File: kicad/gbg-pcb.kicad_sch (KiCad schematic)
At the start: 70 parts, among them J1 12 2.54mm pitch header pins, J100 0197054001, J101 0197054001, J102 0197054001, J103 0197054001, J104 2159151002, J11 Conn_01x10_Pin, J2 Conn_01x04, J3 joystick, J4 speed knob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

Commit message: reviewed
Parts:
- U3: DigiKey_Part_Number 296-44396-1-ND -> (none)
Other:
- moved on the sheet: 3V1, B1, B2, B3, B4, C1, C2, C4, D1, D13, D2, H1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

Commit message: v2.1
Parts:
- R4: value 590k -> 100k; Manufacturer_Part_Number CRCW0805590KFKEA -> CRCW0805100KFKEA; digikey_part_number 541-590KCCT-ND -> 541-100KCCT-ND
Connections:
- net GND: no longer B1.4, B2.4, B3.4, B4.4
- no-connect marks 16 -> 20

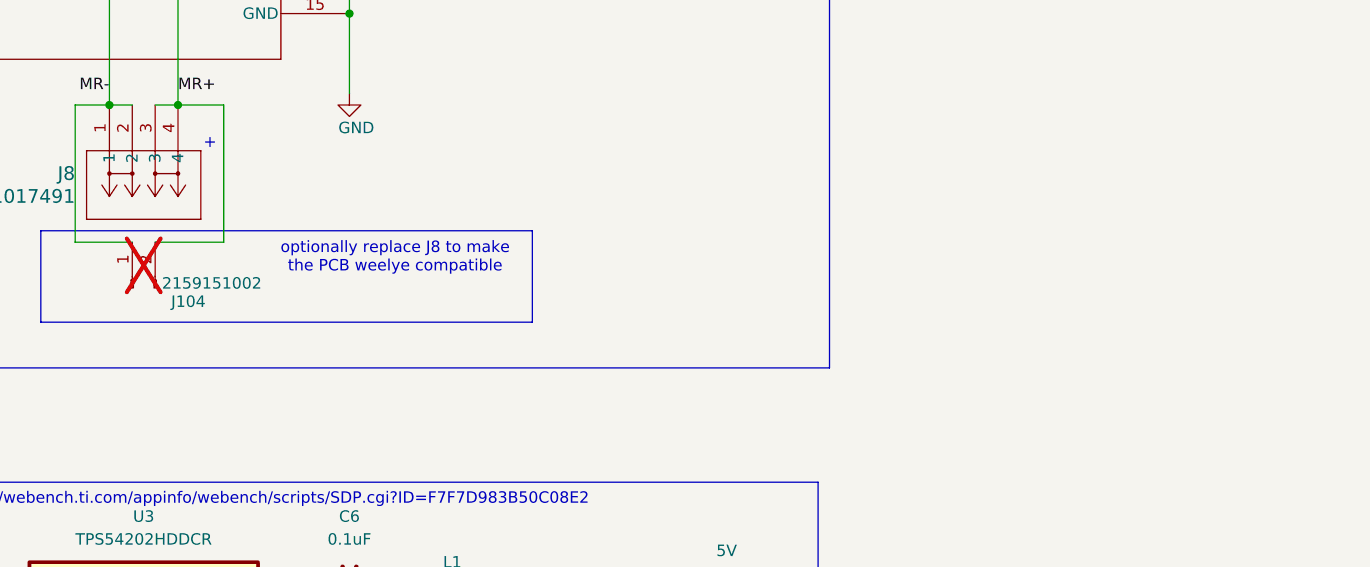
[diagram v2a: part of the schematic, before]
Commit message: add vias
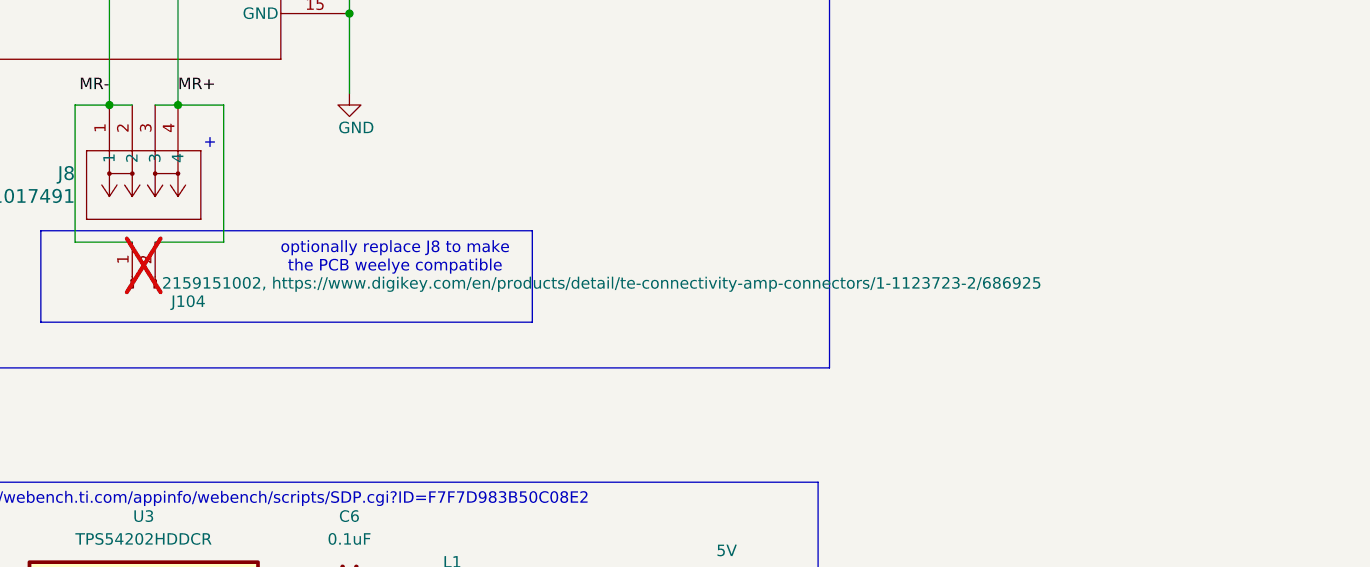
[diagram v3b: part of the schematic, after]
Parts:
- J104: value 2159151002 -> 2159151002, https://www.digikey.com/en/products/detail/te-connectivity-amp-connectors/1-1123723-2/686925
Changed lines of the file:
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@@
 			)
 		)
-		(property "Value" "2159151002"
+		(property "Value" "2159151002, https://www.digikey.com/en/products/detail/te-connectivity-amp-connectors/1-1123723-2/686925"
 			(at 327.152 181.102 90)
 			(show_name no)
@@
 			)
 		)
-		(property "Datasheet" "https://www.digikey.com/en/products/detail/molex/2159151002/16591336"
+		(property "Datasheet" "https://www.digikey.com/en/products/detail/molex/2159151002/16591336, https://www.digikey.com/en/products/detail/te-connectivity-amp-connectors/1-1123723-2/686925"
 			(at 323.85 181.61 0)
 			(hide yes)

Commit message: work on right motor connection
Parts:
- added J105: wellye RX25 style, kicad libraries:TE_1-1123723-2, symbol Connector:Conn_01x02_Pin
- J104: value 2159151002, https://www.digikey.com/en/products/detail/te-connectivity-amp-connectors/1-1123723-2/686925 -> wellye style
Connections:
- net MR+: now also J105.2 (Pin_2)
- net MR-: now also J105.1 (Pin_1)
- net right_1: now also P1.22 (GP17); no longer P1.21 (GP16)
- net right_2: now also P1.21 (GP16); no longer P1.22 (GP17)
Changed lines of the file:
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@@
 	(rectangle
 		(start 313.69 175.26)
-		(end 368.3 185.42)
+		(end 368.3 198.12)
 		(stroke
 			(width 0)
@@
 		)
 	)
-	(text_box "right motor"
-		(exclude_from_sim no)
-		(at 236.22 101.6 0)
-		(size 165.1 88.9)
-		(margins 0.9525 0.9525 0.9525 0.9525)
-		(stroke
-			(width 0)
-			(type solid)
-		)
-		(fill
-			(type none)
-		)
-		(effects
-			(font
-				(size 1.27 1.27)
-			)
-			(justify left top)
-		)
-	)
 	(text_box "qwiic I2C plug"
 		(exclude_from_sim no)
@@
 	)
 	(junction
+		(at 334.01 176.53)
+		(diameter 0)
+		(color 0 0 0 0)
+	)
+	(junction
 		(at 92.71 46.99)
 		(diameter 0)
@@
 	)
 	(junction
+		(at 317.5 176.53)
+		(diameter 0)
+		(color 0 0 0 0)
+	)
+	(junction
 		(at 297.18 50.8)
 		(diameter 0)
@@
 	(wire
 		(pts
+			(xy 317.5 186.69) (xy 317.5 176.53)
+		)
+		(stroke
+			(width 0)
+			(type default)
+		)
+	)
+	(wire
+		(pts
 			(xy 82.55 57.15) (xy 82.55 54.61)
 		)
@@
 	(wire
 		(pts
+			(xy 326.39 186.69) (xy 334.01 186.69)
+		)
+		(stroke
+			(width 0)
+			(type default)
+		)
+	)
+	(wire
+		(pts
 			(xy 102.87 77.47) (xy 102.87 54.61)
 		)
@@
 	(wire
 		(pts
+			(xy 323.85 186.69) (xy 317.5 186.69)
+		)
+		(stroke
+			(width 0)
+			(type default)
+		)
+	)
+	(wire
+		(pts
 			(xy 87.63 74.93) (xy 101.6 74.93)
 		)
@@
 	(wire
 		(pts
+			(xy 334.01 186.69) (xy 334.01 176.53)
+		)
+		(stroke
+			(width 0)
+			(type default)
+		)
+	)
+	(wire
+		(pts
 			(xy 204.47 82.55) (xy 204.47 78.74)
 		)
@@
 		)
 	)
-	(global_label "sda"
+	(global_label "right_1"
 		(shape input)
-		(at 130.81 157.48 180)
+		(at 185.42 67.31 0)
 		(fields_autoplaced yes)
 		(effects
@@
 				(size 1.27 1.27)
 			)
-			(justify right)
+			(justify left)
 		)
 		(property "Intersheetrefs" "${INTERSHEET_REFS}"
-			(at 124.4987 157.48 0)
+			(at 194.997 67.31 0)
 			(hide yes)
 			(show_name no)
@@
 					(size 1.27 1.27)
 				)
-				(justify right)
+				(justify left)
 			)
 		)
 	)
-	(global_label "left_ipropi"
+	(global_label "right_2"
 		(shape input)
-		(at 40.64 172.72 180)
+		(at 185.42 64.77 0)
+		(fields_autoplaced yes)
+		(effects
+			(font
+				(size 1.27 1.27)
+			)
+			(justify left)
+		)
+		(property "Intersheetrefs" "${INTERSHEET_REFS}"
+			(at 194.997 64.77 0)
+			(hide yes)
+			(show_name no)
+			(do_not_autoplace no)
+			(effects
+				(font
+					(size 1.27 1.27)
+				)
+				(justify left)
+			)
+		)
+	)
+	(global_label "sda"
+		(shape input)
+		(at 130.81 157.48 180)
 		(fields_autoplaced yes)
 		(effects
@@
 		)
 		(property "Intersheetrefs" "${INTERSHEET_REFS}"
-			(at 28.0392 172.72 0)
+			(at 124.4987 157.48 0)
 			(hide yes)
 			(show_name no)
@@
 		)
 	)
-	(global_label "right_2"
+	(global_label "left_ipropi"
 		(shape input)
-		(at 297.18 123.19 180)
+		(at 40.64 172.72 180)
 		(fields_autoplaced yes)
 		(effects
@@
 		)
 		(property "Intersheetrefs" "${INTERSHEET_REFS}"
-			(at 287.603 123.19 0)
+			(at 28.0392 172.72 0)
 			(hide yes)
 			(show_name no)
@@
 		)
 	)
-	(global_label "scl"
+	(global_label "right_2"
 		(shape input)
-		(at 97.79 182.88 0)
+		(at 297.18 123.19 180)
 		(fields_autoplaced yes)
 		(effects
@@
 				(size 1.27 1.27)
 			)
-			(justify left)
+			(justify right)
 		)
 		(property "Intersheetrefs" "${INTERSHEET_REFS}"
-			(at 103.5571 182.88 0)
+			(at 287.603 123.19 0)
 			(hide yes)
 			(show_name no)
@@
 					(size 1.27 1.27)
 				)
-				(justify left)
+				(justify right)
 			)
 		)
 	)
-	(global_label "right_2"
+	(global_label "scl"
 		(shape input)
-		(at 185.42 67.31 0)
+		(at 97.79 182.88 0)
 		(fields_autoplaced yes)
 		(effects
@@
 		)
 		(property "Intersheetrefs" "${INTERSHEET_REFS}"
-			(at 194.997 67.31 0)
+			(at 103.5571 182.88 0)
 			(hide yes)
 			(show_name no)
@@
 		)
 	)
-	(global_label "right_1"
-		(shape input)
-		(at 185.42 64.77 0)
-		(fields_autoplaced yes)
-		(effects
-			(font
-				(size 1.27 1.27)
-			)
-			(justify left)
-		)
-		(property "Intersheetrefs" "${INTERSHEET_REFS}"
-			(at 194.997 64.77 0)
-			(hide yes)
-			(show_name no)
-			(do_not_autoplace no)
-			(effects
-				(font
-					(size 1.27 1.27)
-				)
-				(justify left)
-			)
-		)
-	)
 	(global_label "bat-"
 		(shape input)
@@
 			)
 		)
-		(property "Description" "24A screw terminal"
+		(property "Description" "motor screw terminals"
 			(at 321.31 83.82 0)
 			(hide yes)
@@
 			)
 		)
-		(property "Value" "2159151002, https://www.digikey.com/en/products/detail/te-connectivity-amp-connectors/1-1123723-2/686925"
-			(at 327.152 181.102 90)
+		(property "Value" "wellye style"
+			(at 327.914 181.102 90)
 			(show_name no)
 			(do_not_autoplace no)
@@
 			)
 		)
-		(property "Datasheet" "https://www.digikey.com/en/products/detail/molex/2159151002/16591336, https://www.digikey.com/en/products/detail/te-connectivity-amp-connectors/1-1123723-2/686925"
+		(property "Datasheet" "https://www.digikey.com/en/products/detail/molex/2159151002/16591336"
 			(at 323.85 181.61 0)
 			(hide yes)
@@
 	)
 	(symbol
+		(lib_id "Connector:Conn_01x02_Pin")
+		(at 323.85 191.77 90)
+		(unit 1)
+		(body_style 1)
+		(exclude_from_sim no)
+		(in_bom yes)
+		(on_board yes)
+		(in_pos_files yes)
+		(dnp yes)
+		(property "Reference" "J105"
+			(at 328.168 193.294 90)
+			(show_name no)
+			(do_not_autoplace no)
+			(effects
+				(font
+					(size 1.27 1.27)
+				)
+				(justify right)
+			)
+		)
+		(property "Value" "wellye RX25 style"
+			(at 327.914 191.262 90)
+			(show_name no)
+			(do_not_autoplace no)
+			(effects
+				(font
+					(size 1.27 1.27)
+				)
+				(justify right)
+			)
+		)
+		(property "Footprint" "kicad libraries:TE_1-1123723-2"
+			(at 323.85 191.77 0)
+			(hide yes)
+			(show_name no)
+			(do_not_autoplace no)
+			(effects
+				(font
+					(size 1.27 1.27)
+				)
+			)
+		)
+		(property "Datasheet" "https://www.digikey.com/en/products/detail/te-connectivity-amp-connectors/1-1123723-2/686925"
+			(at 323.85 191.77 0)
+			(hide yes)
+			(show_name no)
+			(do_not_autoplace no)
+			(effects
+				(font
+					(size 1.27 1.27)
+				)
+			)
+		)
+		(property "Description" "right motor plug"
+			(at 323.85 191.77 0)
+			(hide yes)
+			(show_name no)
+			(do_not_autoplace no)
+			(effects
+				(font
+					(size 1.27 1.27)
+				)
+			)
+		)
+		(property "Mfr" ""
+			(at 323.85 191.77 0)
+			(hide yes)
+			(show_name no)
+			(do_not_autoplace no)
+			(effects
+				(font
+					(size 1.27 1.27)
+				)
+			)
+		)
+		(property "Mfr PN" ""
+			(at 323.85 191.77 0)
+			(hide yes)
+			(show_name no)
+			(do_not_autoplace no)
+			(effects
+				(font
+					(size 1.27 1.27)
+				)
+			)
+		)
+		(property "Supplier" ""
+			(at 323.85 191.77 0)
+			(hide yes)
+			(show_name no)
+			(do_not_autoplace no)
+			(effects
+				(font
+					(size 1.27 1.27)
+				)
+			)
+		)
+		(property "Supplier PN" ""
+			(at 323.85 191.77 0)
+			(hide yes)
+			(show_name no)
+			(do_not_autoplace no)
+			(effects
+				(font
+					(size 1.27 1.27)
+				)
+			)
+		)
+		(property "Manufacturer_Name" "TE Connectivity AMP Connectors"
+			(at 323.85 191.77 90)
+			(hide yes)
+			(show_name no)
+			(do_not_autoplace no)
+			(effects
+				(font
+					(size 1.27 1.27)
+				)
+			)
+		)
+		(property "Manufacturer_Part_Number" "1-1123723-2"
+			(at 323.85 191.77 90)
+			(hide yes)
+			(show_name no)
+			(do_not_autoplace no)
+			(effects
+				(font
+					(size 1.27 1.27)
+				)
+			)
+		)
+		(property "digikey_part_number" "A111830-ND"
+			(at 323.85 191.77 90)
+			(hide yes)
+			(show_name no)
+			(do_not_autoplace no)
+			(effects
+				(font
+					(size 1.27 1.27)
+				)
+			)
+		)
+		(property "mount_type" "tht"
+			(at 323.85 191.77 90)
+			(hide yes)
+			(show_name no)
+			(do_not_autoplace no)
+			(effects
+				(font
+					(size 1.27 1.27)
+				)
+			)
+		)
+		(property "price" ".2"
+			(at 323.85 191.77 90)
+			(hide yes)
+			(show_name no)
+			(do_not_autoplace no)
+			(effects
+				(font
+					(size 1.27 1.27)
+				)
+			)
+		)
+		(pin "2"
+		)
+		(pin "1"
+		)
+		(instances
+			(project "gbg-pcb"
+				(path "/3bb9adb4-655f-45ab-af84-44b563241ee2"
+					(reference "J105")
+					(unit 1)
+				)
+			)
+		)
+	)
+	(symbol
 		(lib_id "power:+BATT")
 		(at 31.75 148.59 0)
@@
 			)
 		)
-		(property "Description" "24A screw terminal"
+		(property "Description" "motor screw terminals"
 			(at 321.31 161.29 0)
 			(hide yes)

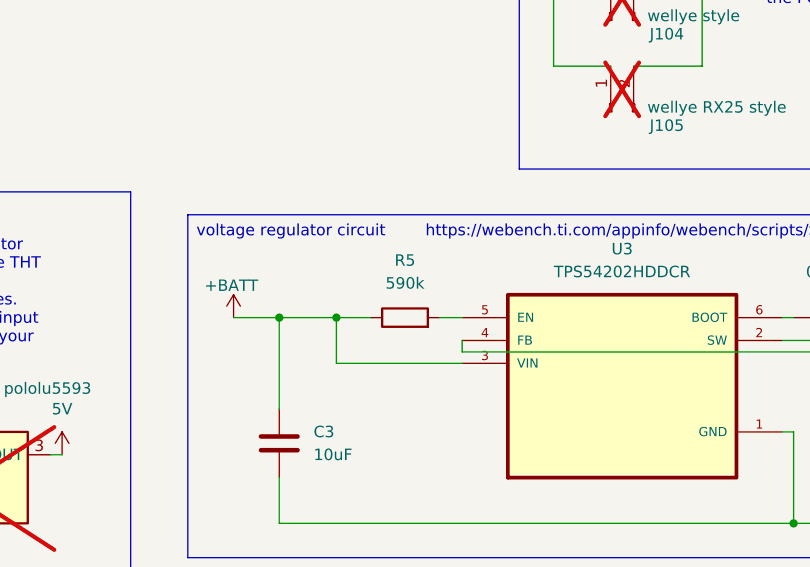
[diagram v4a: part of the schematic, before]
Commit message: updates from assembling V2.1, and silkscreen
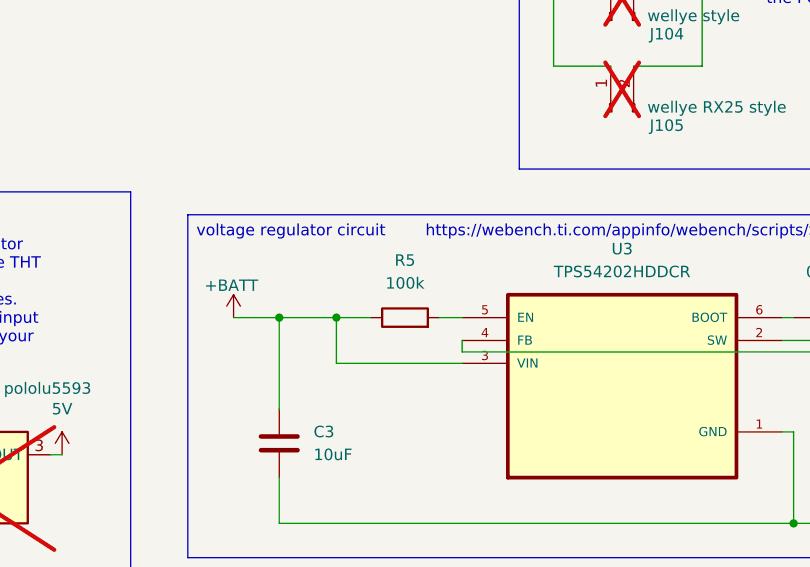
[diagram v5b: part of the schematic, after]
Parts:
- R5: value 590k -> 100k; Manufacturer_Part_Number CRCW0805590KFKEA -> CRCW0805100KFKEA; digikey_part_number 541-590KCCT-ND -> 541-100KCCT-ND
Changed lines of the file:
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@@
 	)
 	(symbol
-		(lib_id "Device:R")
-		(at 300.99 214.63 90)
-		(unit 1)
-		(body_style 1)
-		(exclude_from_sim no)
-		(in_bom yes)
-		(on_board yes)
-		(in_pos_files yes)
-		(dnp no)
-		(fields_autoplaced yes)
-		(property "Reference" "R5"
-			(at 300.99 208.28 90)
-			(show_name no)
-			(do_not_autoplace no)
-			(effects
-				(font
-					(size 1.27 1.27)
-				)
-			)
-		)
-		(property "Value" "590k"
-			(at 300.99 210.82 90)
-			(show_name no)
-			(do_not_autoplace no)
-			(effects
-				(font
-					(size 1.27 1.27)
-				)
-			)
-		)
-		(property "Footprint" "Resistor_SMD:R_0805_2012Metric"
-			(at 300.99 216.408 90)
-			(hide yes)
-			(show_name no)
-			(do_not_autoplace no)
-			(effects
-				(font
-					(size 1.27 1.27)
-				)
-			)
-		)
-		(property "Datasheet" "https://www.digikey.com/en/products/detail/vishay-dale/CRCW0805590KFKEA/1175990"
-			(at 300.99 214.63 0)
-			(hide yes)
-			(show_name no)
-			(do_not_autoplace no)
-			(effects
-				(font
-					(size 1.27 1.27)
-				)
-			)
-		)
-		(property "Description" "enable pull up"
-			(at 300.99 214.63 0)
-			(hide yes)
-			(show_name no)
-			(do_not_autoplace no)
-			(effects
-				(font
-					(size 1.27 1.27)
-				)
-			)
-		)
-		(property "Manufacturer_Name" "Vishay Dale"
-			(at 300.99 214.63 90)
-			(hide yes)
-			(show_name no)
-			(do_not_autoplace no)
-			(effects
-				(font
-					(size 1.27 1.27)
-				)
-			)
-		)
-		(property "Manufacturer_Part_Number" "CRCW0805590KFKEA"
-			(at 300.99 214.63 90)
-			(hide yes)
-			(show_name no)
-			(do_not_autoplace no)
-			(effects
-				(font
-					(size 1.27 1.27)
-				)
-			)
-		)
-		(property "digikey_part_number" "541-590KCCT-ND"
-			(at 300.99 214.63 90)
-			(hide yes)
-			(show_name no)
-			(do_not_autoplace no)
-			(effects
-				(font
-					(size 1.27 1.27)
-				)
-			)
-		)
-		(property "mount_type" "smd"
-			(at 300.99 214.63 90)
-			(hide yes)
-			(show_name no)
-			(do_not_autoplace no)
-			(effects
-				(font
-					(size 1.27 1.27)
-				)
-			)
-		)
-		(property "price" ".04"
-			(at 300.99 214.63 90)
-			(hide yes)
-			(show_name no)
-			(do_not_autoplace no)
-			(effects
-				(font
-					(size 1.27 1.27)
-				)
-			)
-		)
-		(property "Mfr" ""
-			(at 300.99 214.63 0)
-			(hide yes)
-			(show_name no)
-			(do_not_autoplace no)
-			(effects
-				(font
-					(size 1.27 1.27)
-				)
-			)
-		)
-		(property "Mfr PN" ""
-			(at 300.99 214.63 0)
-			(hide yes)
-			(show_name no)
-			(do_not_autoplace no)
-			(effects
-				(font
-					(size 1.27 1.27)
-				)
-			)
-		)
-		(property "Supplier" ""
-			(at 300.99 214.63 0)
-			(hide yes)
-			(show_name no)
-			(do_not_autoplace no)
-			(effects
-				(font
-					(size 1.27 1.27)
-				)
-			)
-		)
-		(property "Supplier PN" ""
-			(at 300.99 214.63 0)
-			(hide yes)
-			(show_name no)
-			(do_not_autoplace no)
-			(effects
-				(font
-					(size 1.27 1.27)
-				)
-			)
-		)
-		(pin "2"
-		)
-		(pin "1"
-		)
-		(instances
-			(project "gbg-pcb"
-				(path "/3bb9adb4-655f-45ab-af84-44b563241ee2"
-					(reference "R5")
-					(unit 1)
-				)
-			)
-		)
-	)
-	(symbol
 		(lib_id "library:ASJ-200-B-HT")
 		(at 55.88 208.28 0)
@@
 					(unit 1)
 				)
+			)
+		)
+	)
+	(symbol
+		(lib_id "Device:R")
+		(at 300.99 214.63 90)
+		(unit 1)
+		(body_style 1)
+		(exclude_from_sim no)
+		(in_bom yes)
+		(on_board yes)
+		(in_pos_files yes)
+		(dnp no)
+		(fields_autoplaced yes)
+		(property "Reference" "R5"
+			(at 300.99 208.28 90)
+			(show_name no)
+			(do_not_autoplace no)
+			(effects
+				(font
+					(size 1.27 1.27)
+				)
+			)
+		)
+		(property "Value" "100k"
+			(at 300.99 210.82 90)
+			(show_name no)
+			(do_not_autoplace no)
+			(effects
+				(font
+					(size 1.27 1.27)
+				)
+			)
+		)
+		(property "Footprint" "Resistor_SMD:R_0805_2012Metric"
+			(at 300.99 216.408 90)
+			(hide yes)
+			(show_name no)
+			(do_not_autoplace no)
+			(effects
+				(font
+					(size 1.27 1.27)
+				)
+			)
+		)
+		(property "Datasheet" "https://www.digikey.com/en/products/detail/vishay-dale/CRCW0805100KFKEA/1181013"
+			(at 300.99 214.63 0)
+			(hide yes)
+			(show_name no)
+			(do_not_autoplace no)
+			(effects
+				(font
+					(size 1.27 1.27)
+				)
+			)
+		)
+		(property "Description" "Rfbt"
+			(at 300.99 214.63 0)
+			(hide yes)
+			(show_name no)
+			(do_not_autoplace no)
+			(effects
+				(font
+					(size 1.27 1.27)
+				)
+			)
+		)
+		(property "Manufacturer_Name" "Vishay Dale"
+			(at 300.99 214.63 0)
+			(hide yes)
+			(show_name no)
+			(do_not_autoplace no)
+			(effects
+				(font
+					(size 1.27 1.27)
+				)
+			)
+		)
+		(property "Manufacturer_Part_Number" "CRCW0805100KFKEA"
+			(at 300.99 214.63 0)
+			(hide yes)
+			(show_name no)
+			(do_not_autoplace no)
+			(effects
+				(font
+					(size 1.27 1.27)
+				)
+			)
+		)
+		(property "mount_type" "smd"
+			(at 300.99 214.63 0)
+			(hide yes)
+			(show_name no)
+			(do_not_autoplace no)
+			(effects
+				(font
+					(size 1.27 1.27)
+				)
+			)
+		)
+		(property "digikey_part_number" "541-100KCCT-ND"
+			(at 300.99 214.63 0)
+			(hide yes)
+			(show_name no)
+			(do_not_autoplace no)
+			(effects
+				(font
+					(size 1.27 1.27)
+				)
+			)
+		)
+		(property "price" ".04"
+			(at 300.99 214.63 0)
+			(hide yes)
+			(show_name no)
+			(do_not_autoplace no)
+			(effects
+				(font
+					(size 1.27 1.27)
+				)
+			)
+		)
+		(property "Mfr" ""
+			(at 300.99 214.63 0)
+			(hide yes)
+			(show_name no)
+			(do_not_autoplace no)
+			(effects
+				(font
+					(size 1.27 1.27)
+				)
+			)
+		)
+		(property "Mfr PN" ""
+			(at 300.99 214.63 0)
+			(hide yes)
+			(show_name no)
+			(do_not_autoplace no)
+			(effects
+				(font
+					(size 1.27 1.27)
+				)
+			)
+		)
+		(property "Supplier" ""
+			(at 300.99 214.63 0)
+			(hide yes)
+			(show_name no)
+			(do_not_autoplace no)
+			(effects
+				(font
+					(size 1.27 1.27)
+				)
+			)
+		)
+		(property "Supplier PN" ""
+			(at 300.99 214.63 0)
+			(hide yes)
+			(show_name no)
+			(do_not_autoplace no)
+			(effects
+				(font
+					(size 1.27 1.27)
+				)
+			)
+		)
+		(pin "2"
+		)
+		(pin "1"
+		)
+		(instances
+			(project "gbg-pcb"
+				(path "/3bb9adb4-655f-45ab-af84-44b563241ee2"
+					(reference "R5")
+					(unit 1)
+				)

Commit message: arrange
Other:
- note removed: "1.8-5.5v"
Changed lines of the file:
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@@
 		)
 	)
-	(text "1.8-5.5v"
-		(exclude_from_sim no)
-		(at 171.958 20.574 0)
-		(effects
-			(font
-				(size 1.27 1.27)
-			)
-		)
-	)
 	(text "on/off switch"
 		(exclude_from_sim no)
@@
 		)
 		(property "Value" "screw terminal"
-			(at 151.384 241.808 0)
+			(at 148.082 242.062 0)
 			(show_name no)
 			(do_not_autoplace no)
